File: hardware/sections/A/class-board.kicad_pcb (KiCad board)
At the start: 4 copper layers, 180 x 100 mm, 334 parts, among them J1 DevKit J1 (left row), J10 C2937625_-_Conn_01x03, J11 C2937625_-_Conn_01x03, J12 C2937625_-_Conn_01x03, J13 C492401-PZ254V-11-02P, J14 C2937625_-_Conn_01x03, J15 C2937625_-_Conn_01x03, J2 DevKit J3 (right row), J201 USB-C 16P, J202 DC005-T20, J3 C2937625_-_Conn_01x03, J4 Qwiic, J5 Expansion 2x10, J6 Panel link 2x20 female, J7 Panel link 2x20 female, J8 Panel link 2x20 female, J9 C2937625_-_Conn_01x03, J901 KF301-5.0-2P, J903 KF301-5.0-2P, J905 KF301-5.0-3P, Q901 AOD4185, Q904 AOD4184A, U101 ADS8688IDBTR, U201 LM66100DCKR, U202 LM66100DCKR, U203 78L05G-AB3-R, U204 AMS1117-3.3, U301 DAC8563SDGSR, U302 74HCT125PW, U303 OPA2192IDR, U501 SN74AHCT541PWR, U502 74HCT125PW, U503 SN74LVC1T45DBVR, U505 TCA9535PWR, U701 SI5351A-B-GT, U702 74HC74D,653, U703 OPA1656IDR, U704 DG419DY-T1-E3, U705 OPA1612AIDR, U706 OPA1612AIDR, U801 AD9834BRUZ, U802 OPA564AIDWPR, U901 TS5A23157DGSR, U902 TS5A23157DGSR, U903 DRV8871DDAR, U904 UCC27517DBVR, Y701 25 MHz

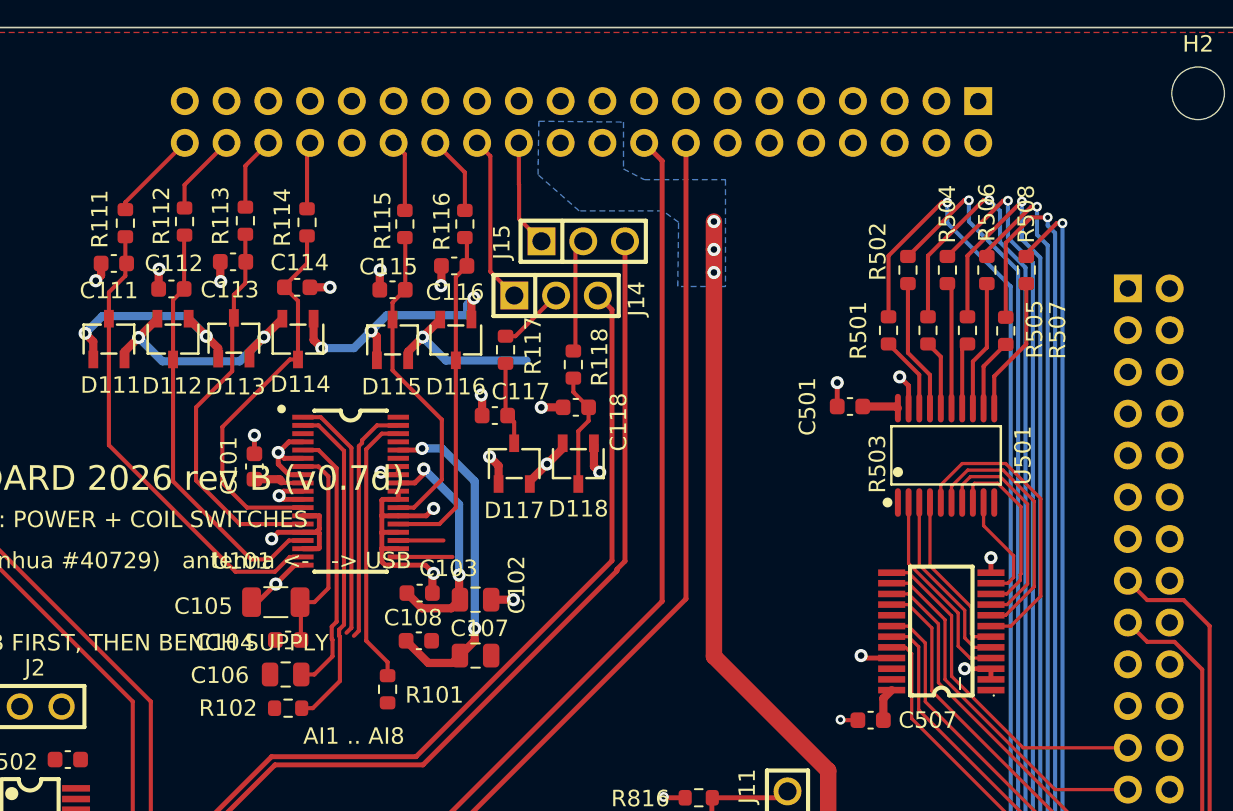
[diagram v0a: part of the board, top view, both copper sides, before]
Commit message: main board area A: route 47 of the 53 connections inside ZONE_A
402 tracks and 16 vias added inside the ZONE_A rule area. DRC against the
copy as handed out: no new violation of any kind. Every count matches the
baseline exactly (silk 16/13, track_dangling 10, lib_footprint_mismatch 7,
isolated_copper 1) and via_dangling improves 47 -> 45. No footprint moved,
no zone changed, nothing on an inner layer, nothing outside ZONE_A, and the
instructor's locked routing untouched.

Six connections are left unrouted, and they are not arbitrary:

- Five sit around U101, a TSSOP-38 on 0.5 mm pitch. Measured at U101 pad 8,
  a +-1 mm window has 19 free cells on F.Cu against 1485 on B.Cu: the pad is
  walled in on the top layer by its neighbours' clearance, the bottom layer
  is wide open, but the nearest legal via is 3 mm away with no corridor on
  F.Cu to reach it. analog_in_clearance (0.3 mm from an AIN track to anything
  but AGND) closes what little is left. This needs a part moved or a decision
  from the instructor, not a cleverer search.
- +5V_RAW at U501 can be routed, but only along a path that comes within
  0.068 mm of U501 pad 19 against a 0.2 mm rule. Left unrouted on purpose:
  DRC-clean matters more here than one more connection.

Notes on how the tracks were produced, since the geometry should be
explainable: a grid A* on 0.05 mm cells over the existing copper, then each
run split into chunks using at most two step directions and redrawn as one
45-degree diagonal plus one orthogonal leg, each shortcut re-verified cell by
cell. That is what keeps this at 402 segments averaging 0.81 mm rather than
the 852 averaging 0.39 mm a naive merge gives. The fragments that remain are
around U101, where the gaps between pads genuinely are that narrow.

Co-Authored-By: Claude Opus 5 (1M context) <noreply@anthropic.com>
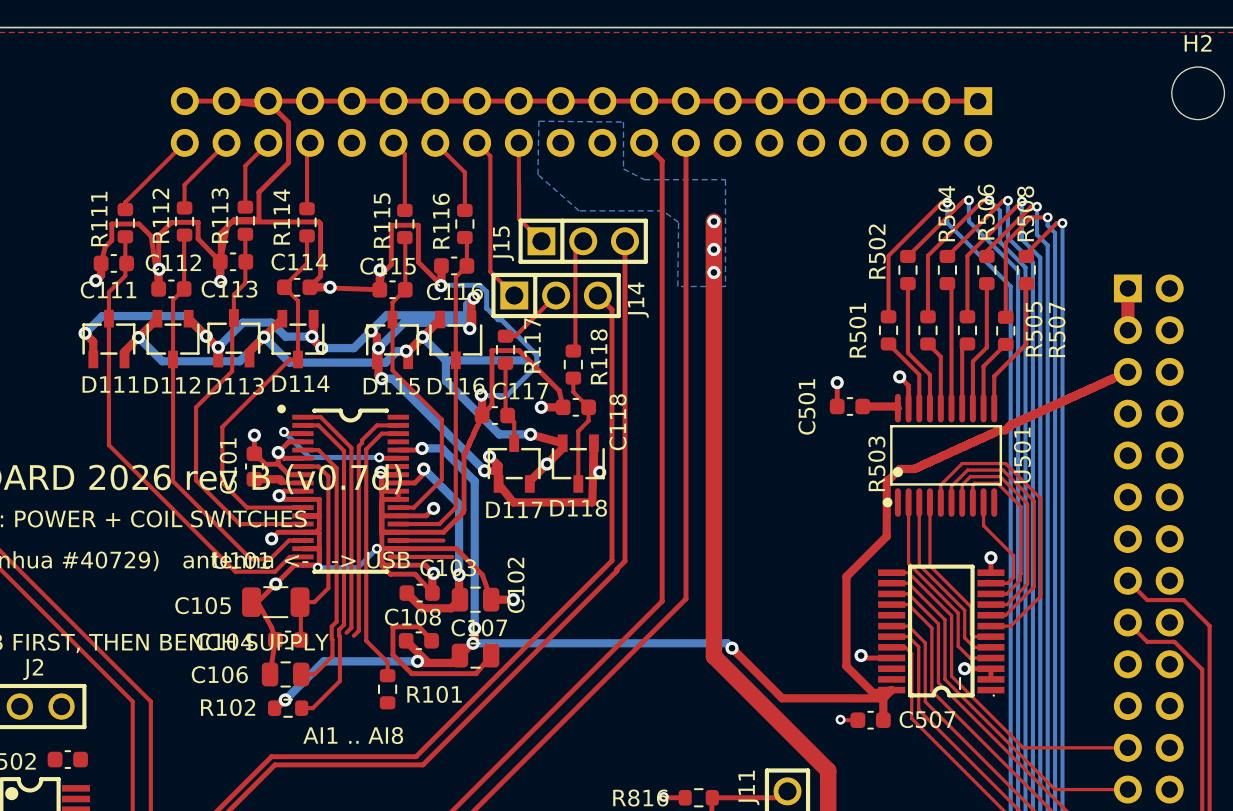
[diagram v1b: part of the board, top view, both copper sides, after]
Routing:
- net AGND: track 162.8 -> 343.1 mm, vias 87 -> 89
- net +3V3: track 77.5 -> 147.6 mm, vias 6 -> 10
- net -12V: track 80.5 -> 115.1 mm, vias 11 -> 17
- net GND: track 135.3 -> 155.5 mm, vias 68 -> 70
- net +12V: track 94.6 -> 114.1 mm, vias 9 -> 11
- net +5V_RAW: track 86.6 -> 89.1 mm

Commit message: Merge student A (Renqian): area A of the main board (417 tracks/vias, unconnected 197 -> 148) and panel section A (13 analog nets, 121 unconnected left) accepted into the masters; sections re-split
Co-Authored-By: Claude Fable 5.1 <noreply@anthropic.com>
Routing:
- net AGND: track 343.1 -> 342.1 mm

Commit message: Main board: five copper zones restored (missing from the 2026-09-24 save), student A's area-A routing accepted (26 items; 157 unconnected); Decision #70: three students on the boards (A Renqian, B Yi-Tsai, C instructor, D Lihdong) in both sections READMEs; sections re-split
Co-Authored-By: Claude Fable 5.1 <noreply@anthropic.com>
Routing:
- net AGND: track 342.1 -> 312.6 mm, vias 89 -> 87
- net +5V_RAW: track 89.1 -> 108.1 mm, vias 0 -> 3
- net /b1_inputs/CS_ADC: track 0.00 -> 10.8 mm
- net +5VA: track 34.4 -> 44.9 mm, vias 2 -> 3
- net GND: track 155.5 -> 154.3 mm, vias 70 -> 86
